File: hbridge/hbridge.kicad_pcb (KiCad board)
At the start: 2 copper layers, 164.5 x 116.5 mm, 8 parts, among them J1 MOSFET1, J2 MOSFET1, J3 MOSFET1, J4 MOSFET1, J5 Driver_in, J6 Driver_in, J7 Driver_in, J8 Driver_in

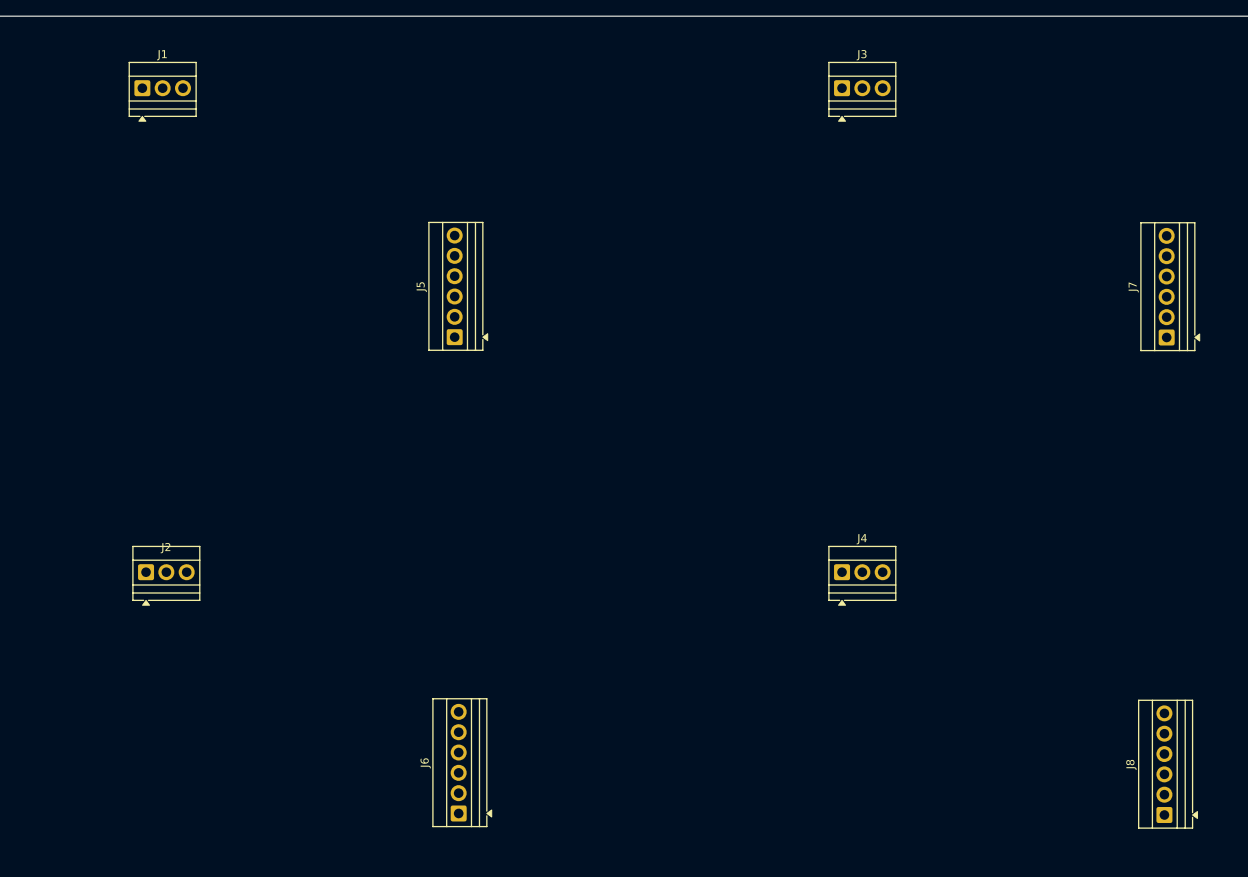
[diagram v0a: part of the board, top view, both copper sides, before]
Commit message: Drivers added to half-bridge.
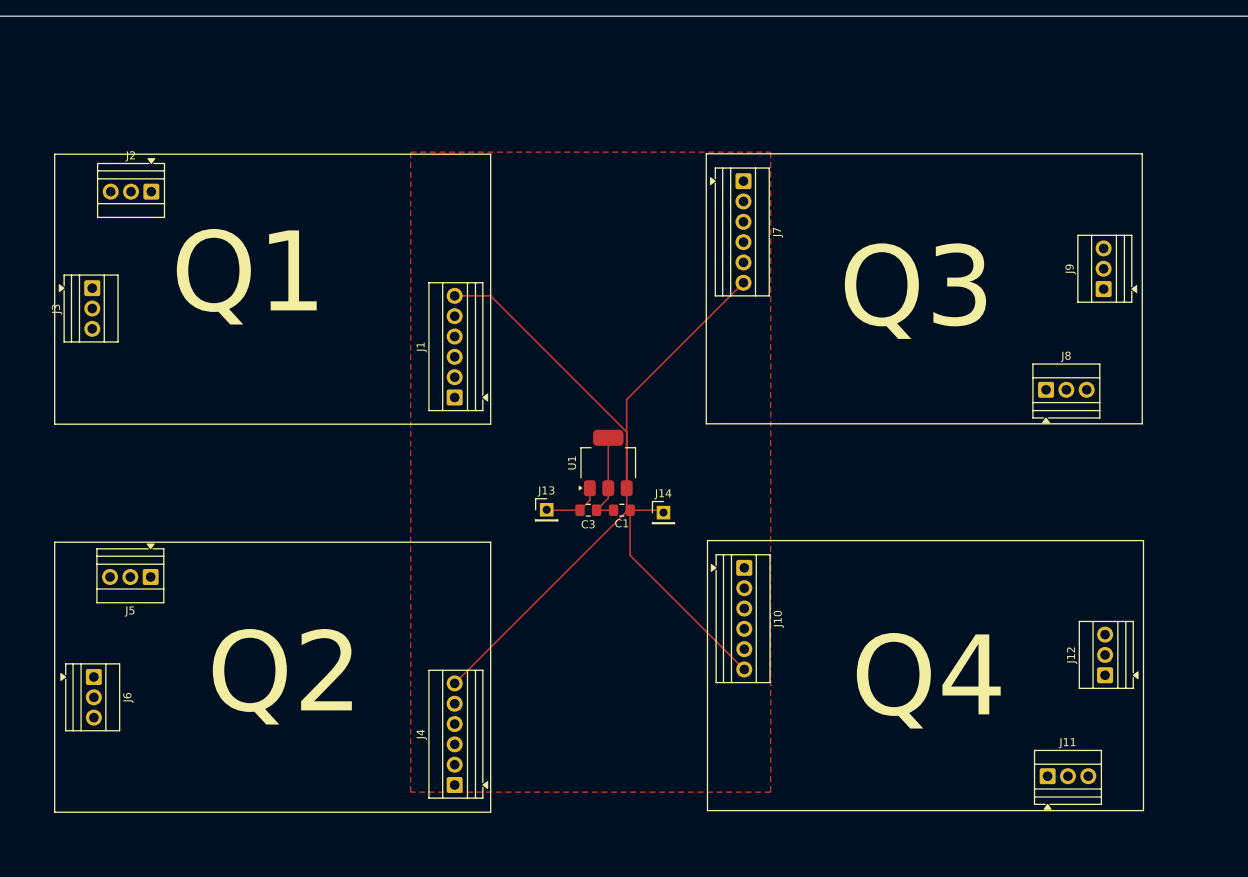
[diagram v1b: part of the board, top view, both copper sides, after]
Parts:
- added C1: C, Capacitor_SMD:C_0805_2012Metric_Pad1.18x1.45mm_HandSolder, F.Cu at (151.4, 84.8)
- added C3: C, Capacitor_SMD:C_0805_2012Metric_Pad1.18x1.45mm_HandSolder, F.Cu at (147.2, 84.8)
- added J10: From_MCU, TerminalBlock:TerminalBlock_Xinya_XY308-2.54-6P_1x06_P2.54mm_Horizontal, F.Cu at (166.7, 92.0)
- added J11: MOSFET_out, TerminalBlock:TerminalBlock_Xinya_XY308-2.54-3P_1x03_P2.54mm_Horizontal, F.Cu at (204.6, 118.0)
- added J12: Conn_01x03, TerminalBlock:TerminalBlock_Xinya_XY308-2.54-3P_1x03_P2.54mm_Horizontal, F.Cu at (211.8, 105.4)
- added J13: Conn_01x01_Socket, Connector_PinHeader_2.54mm:PinHeader_1x01_P2.54mm_Vertical, F.Cu at (142.0, 84.7)
- added J14: Conn_01x01_Socket, Connector_PinHeader_2.54mm:PinHeader_1x01_P2.54mm_Vertical, F.Cu at (156.6, 85.0)
- added J9: Conn_01x03, TerminalBlock:TerminalBlock_Xinya_XY308-2.54-3P_1x03_P2.54mm_Horizontal, F.Cu at (211.6, 57.1)
- added U1: LDO-3.3, Package_TO_SOT_SMD:SOT-223-3_TabPin2, F.Cu at (149.7, 78.8)
- J1, J4: value MOSFET1 -> From_MCU; footprint TerminalBlock:TerminalBlock_Xinya_XY308-2.54-3P_1x03_P2.54mm_Horizontal -> TerminalBlock:TerminalBlock_Xinya_XY308-2.54-6P_1x06_P2.54mm_Horizontal
- J2: value MOSFET1 -> MOSFET_out
- J3: value MOSFET1 -> Conn_01x03
- J5, J8: value Driver_in -> MOSFET_out; footprint TerminalBlock:TerminalBlock_Xinya_XY308-2.54-6P_1x06_P2.54mm_Horizontal -> TerminalBlock:TerminalBlock_Xinya_XY308-2.54-3P_1x03_P2.54mm_Horizontal
- J6: value Driver_in -> Conn_01x03; footprint TerminalBlock:TerminalBlock_Xinya_XY308-2.54-6P_1x06_P2.54mm_Horizontal -> TerminalBlock:TerminalBlock_Xinya_XY308-2.54-3P_1x03_P2.54mm_Horizontal
- J7: value Driver_in -> From_MCU
- moved J3 97.0 mm to (85.2, 57.0), turned to -90 degrees
- moved J7 56.4 mm to (166.6, 43.6), turned to -90 degrees
- moved J4 55.2 mm to (130.5, 119.1), turned to 90 degrees
- moved J8 55.2 mm to (204.4, 69.7), turned to 0 degrees
- moved J1 54.9 mm to (130.5, 70.7), turned to 90 degrees
- moved J6 48.7 mm to (85.4, 105.6), turned to -90 degrees
- moved J5 48.4 mm to (92.5, 93.1), turned to 180 degrees
- moved J2 47.6 mm to (92.6, 44.9), turned to 180 degrees
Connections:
- net Net-(J1-Pin_2) renamed /IN1
- net Net-(J2-Pin_2) renamed /drain1
- net Net-(J4-Pin_2) renamed /IN2
- J1 pad 1: Net-(J1-Pin_1) -> GND_DRV1
- J1 pad 3: Net-(J1-Pin_3) -> /RDY1
- J2 pad 1: Net-(J2-Pin_1) -> /gate1
- J2 pad 3: Net-(J1-Pin_3) -> GND_DRV2
- J3 pad 1: Net-(J3-Pin_1) -> +15_DRV2
- J3 pad 2: Net-(J3-Pin_2) -> GND_DRV2
- J3 pad 3: Net-(J3-Pin_3) -> -15_DRV2
- J4 pad 1: Net-(J4-Pin_1) -> GND_DRV1
- J4 pad 3: Net-(J3-Pin_3) -> /RDY2
- J5 pad 1: unconnected-(J5-Pin_1-Pad1) -> /gate2
- J5 pad 2: Net-(J1-Pin_1) -> /drain2
- J5 pad 3: unconnected-(J5-Pin_3-Pad3) -> GND_DRV2
- J6 pad 1: unconnected-(J6-Pin_1-Pad1) -> +15_DRV2
- J6 pad 2: Net-(J2-Pin_1) -> GND_DRV2
- J6 pad 3: unconnected-(J6-Pin_3-Pad3) -> -15_DRV2
- J7 pad 1: unconnected-(J7-Pin_1-Pad1) -> GND_DRV1
- J7 pad 2: Net-(J3-Pin_1) -> /IN3
- J7 pad 3: unconnected-(J7-Pin_3-Pad3) -> /RDY3
- J7 pad 4: unconnected-(J7-Pin_4-Pad4) -> /FLT3
- J7 pad 5: unconnected-(J7-Pin_5-Pad5) -> /EN3
- J7 pad 6: unconnected-(J7-Pin_6-Pad6) -> +3V3_DRV1
- J8 pad 1: unconnected-(J8-Pin_1-Pad1) -> /gate3
- J8 pad 2: Net-(J4-Pin_1) -> /drain3
- J8 pad 3: unconnected-(J8-Pin_3-Pad3) -> GND_DRV2
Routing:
- net +3V3_DRV1: track 0.00 -> 131.2 mm
- net GND_DRV1: track 0.00 -> 11.8 mm
- net Net-(J13-Pin_1): track 0.00 -> 7.45 mm
- added copper zone on F.Cu, net GND_DRV1
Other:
- board text added: "Q1"
- board text added: "Q2"
- board text added: "Q3"
- board text added: "Q4"

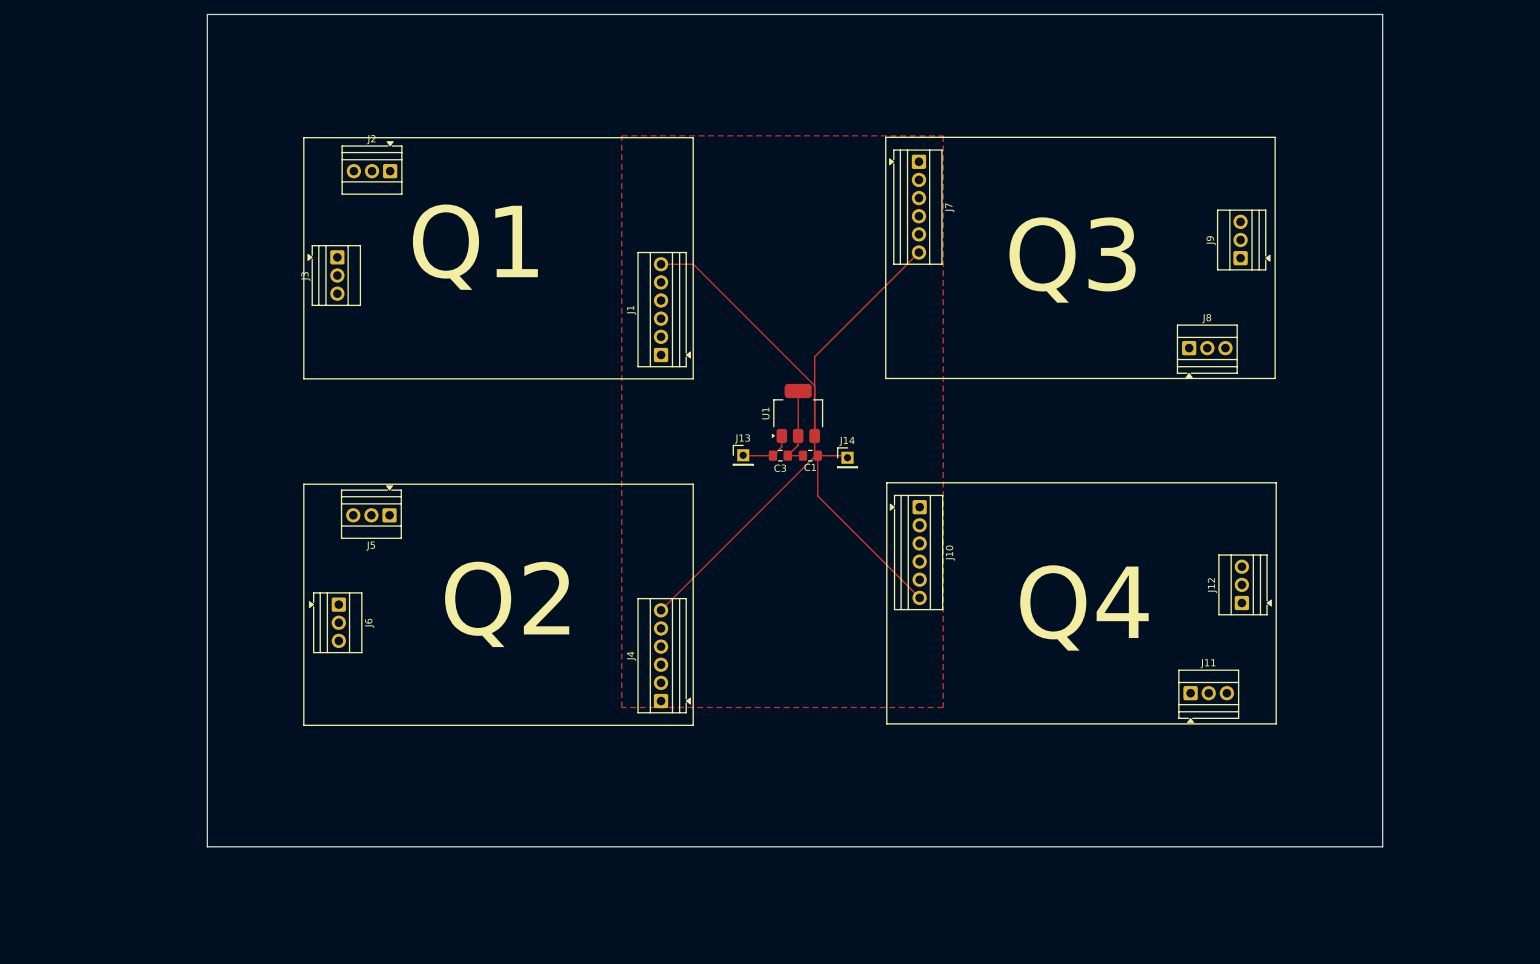
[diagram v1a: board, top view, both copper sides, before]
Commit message: Half bridge power to PCB added.
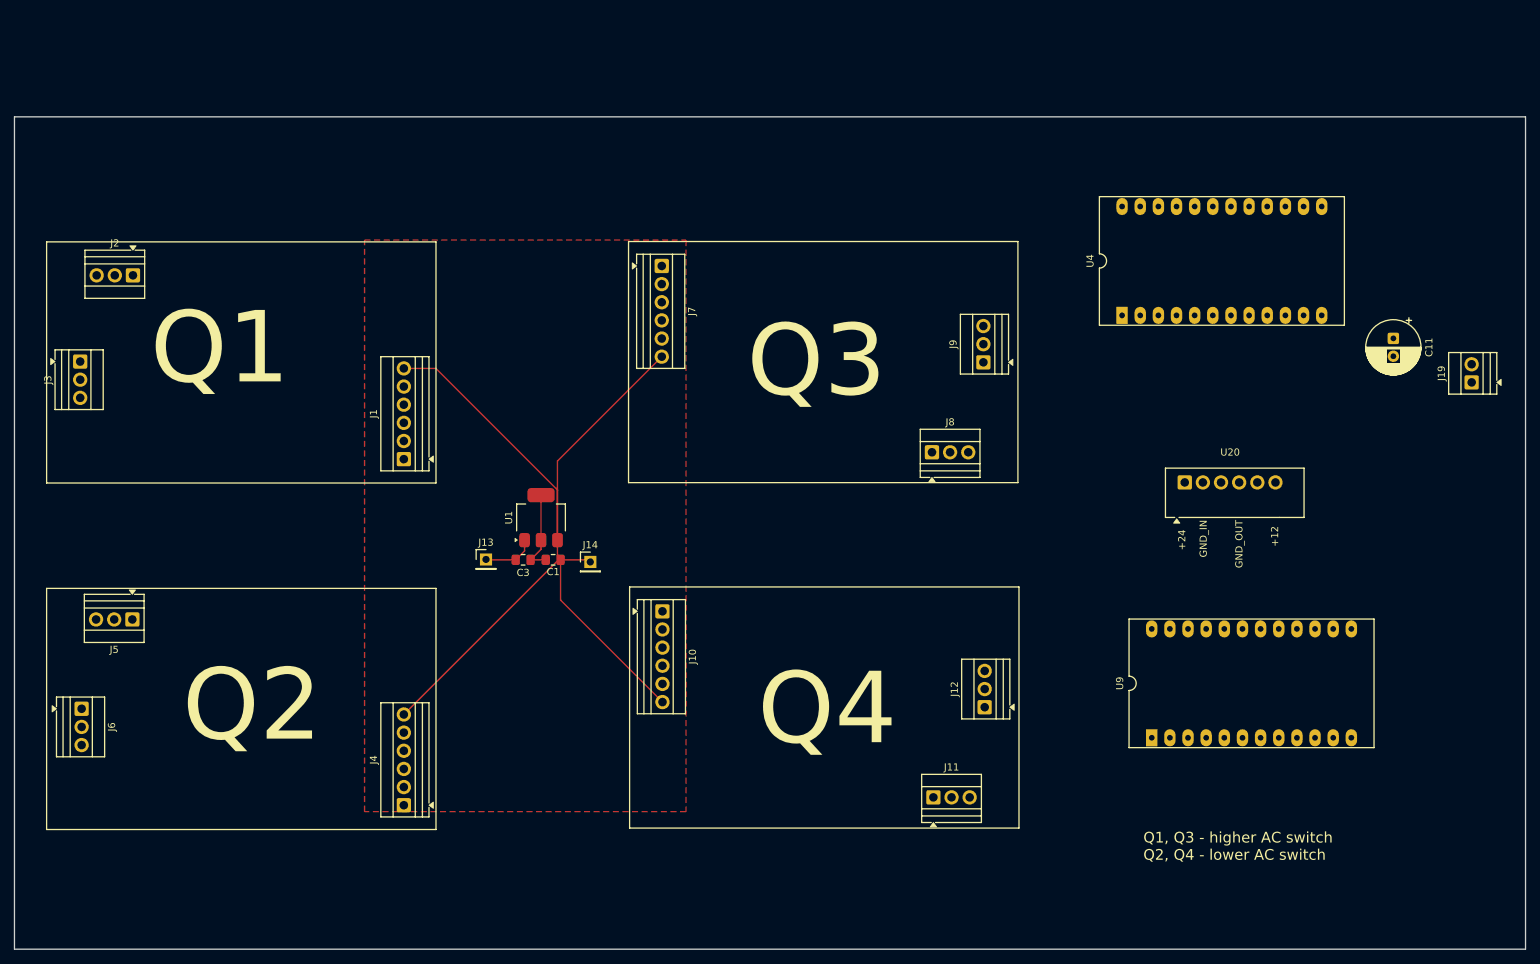
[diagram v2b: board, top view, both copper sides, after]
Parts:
- added C11: 100-220uF/50V, Capacitor_THT:CP_Radial_D7.5mm_P2.50mm, F.Cu at (233.0, 68.3)
- added J19: 24V, TerminalBlock:TerminalBlock_Xinya_XY308-2.54-2P_1x02_P2.54mm_Horizontal, F.Cu at (244.0, 74.5)
- added U20: B2412S-2WR3, TerminalBlock:TerminalBlock_Xinya_XY308-2.54-6P_1x06_P2.54mm_Horizontal, F.Cu at (203.8, 88.5)
- added U4: AM6TW-2415DZ, Package_DIP:DIP-24_18.0mmx34.29mm_W15.24mm_LongPads, F.Cu at (195.0, 65.1)
- added U9: AM6TW-2415DZ, Package_DIP:DIP-24_18.0mmx34.29mm_W15.24mm_LongPads, F.Cu at (199.2, 124.2)
- moved J6 38.8 mm to (49.4, 120.2)
- moved C1 38.8 mm to (115.4, 99.3)
- moved J1 38.8 mm to (94.5, 85.2)
- moved J10 38.8 mm to (130.7, 106.5)
- moved J11 38.8 mm to (168.6, 132.6)
- moved J12 38.8 mm to (175.8, 120.0)
- moved J13 38.8 mm to (106.0, 99.3)
- moved J14 38.8 mm to (120.6, 99.6)
- moved J3 38.8 mm to (49.2, 71.6)
- moved J4 38.8 mm to (94.5, 133.7)
- moved J5 38.8 mm to (56.5, 107.7)
- moved J7 38.8 mm to (130.6, 58.2)
- moved J8 38.8 mm to (168.4, 84.3)
- moved J9 38.8 mm to (175.6, 71.7)
- moved J2 38.8 mm to (56.6, 59.5)
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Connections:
- net /EN1 renamed /драйверы/EN1
- net /EN2 renamed /драйверы/EN2
- net /EN3 renamed /драйверы/EN3
- net /EN4 renamed /драйверы/EN4
- net /FLT1 renamed /драйверы/FLT1
- net /FLT2 renamed /драйверы/FLT2
- net /FLT3 renamed /драйверы/FLT3
- net /FLT4 renamed /драйверы/FLT4
- net /IN1 renamed /драйверы/IN1
- net /IN2 renamed /драйверы/IN2
- net /IN3 renamed /драйверы/IN3
- net /IN4 renamed /драйверы/IN4
- net /RDY1 renamed /драйверы/RDY1
- net /RDY2 renamed /драйверы/RDY2
- net /RDY3 renamed /драйверы/RDY3
- net /RDY4 renamed /драйверы/RDY4
- net /drain1 renamed /драйверы/drain1
- net /drain2 renamed /драйверы/drain2
- net /drain3 renamed /драйверы/drain3
- net /drain4 renamed /драйверы/drain4
- net /gate1 renamed /драйверы/gate1
- net /gate2 renamed /драйверы/gate2
- net /gate3 renamed /драйверы/gate3
- net /gate4 renamed /драйверы/gate4
- net Net-(J13-Pin_1) renamed +12V
- J12 pad 1: +15_DRV2 -> +15_DRV2_L
- J12 pad 2: GND_DRV2 -> GND_DRV2_L
- J12 pad 3: -15_DRV2 -> -15_DRV2_L
- J3 pad 1: +15_DRV2 -> +15_DRV2_H
- J3 pad 2: GND_DRV2 -> GND_DRV2_H
- J3 pad 3: -15_DRV2 -> -15_DRV2_H
- J6 pad 1: +15_DRV2 -> +15_DRV2_L
- J6 pad 2: GND_DRV2 -> GND_DRV2_L
- J6 pad 3: -15_DRV2 -> -15_DRV2_L
- J9 pad 1: +15_DRV2 -> +15_DRV2_H
- J9 pad 2: GND_DRV2 -> GND_DRV2_H
- J9 pad 3: -15_DRV2 -> -15_DRV2_H
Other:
- board size 164.5 x 116.5 mm -> 211.5 x 116.5 mm
- board text added: "+12"
- board text added: "+24"
- board text added: "GND_IN"
- board text added: "GND_OUT"
- board text added: "Q1, Q3 - higher AC switch Q2, Q4 - lower AC switch"

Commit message: PCB minor changes.
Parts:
- moved C11 20.2 mm to (226.0, 87.2)
- moved J19 15.3 mm to (243.2, 89.8)
- moved U20 13.5 mm to (191.6, 94.2)
- moved U9 7.70 mm to (191.5, 125.1)
- moved U4 3.54 mm to (191.5, 65.6)
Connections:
- J11 pad 3: GND_DRV2 -> GND_DRV2_L
- J2 pad 3: GND_DRV2 -> GND_DRV2_H
- J5 pad 3: GND_DRV2 -> GND_DRV2_L
- J8 pad 3: GND_DRV2 -> GND_DRV2_H
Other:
- board size 211.5 x 116.5 mm -> 211.5 x 106.7 mm
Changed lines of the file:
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@@
 			(layers "*.Cu" "*.Mask")
 			(remove_unused_layers no)
-			(net "GND_DRV2")
+			(net "GND_DRV2_H")
 			(pinfunction "Pin_3_3")
 			(pintype "passive")
@@
 	(footprint "TerminalBlock:TerminalBlock_Xinya_XY308-2.54-2P_1x02_P2.54mm_Horizontal"
 		(layer "F.Cu")
-		(at 243.96 74.5 90)
+		(at 243.2175 89.775 90)
 		(descr "Terminal Block Xinya XY308-2.54-2P, 2 pins, pitch 2.54mm, size 5.58x6.5mm, drill diameter 1.2mm, pad diameter 2mm, http://www.xinyaelectronic.com/product/xy308-254")
 		(tags "THT Terminal Block Xinya XY308-2.54-2P pitch 2.54mm size 5.58x6.5mm drill 1.2mm pad 2mm")
@@
 			(layers "*.Cu" "*.Mask")
 			(remove_unused_layers no)
-			(net "GND_DRV2")
+			(net "GND_DRV2_L")
 			(pinfunction "Pin_3_3")
 			(pintype "passive")
@@
 	(footprint "Package_DIP:DIP-24_18.0mmx34.29mm_W15.24mm_LongPads"
 		(layer "F.Cu")
-		(at 199.18 124.24 90)
+		(at 191.53 125.12 90)
 		(descr "24-lead though-hole mounted DIP package, row spacing 15.24 mm (600 mils) https://www.mouser.at/datasheet/2/389/m48t02-1849963.pdf")
 		(tags "THT DIP DIL PDIP 2.54mm 15.24mm 600mil PCDIP24 CAPHAT M48T02 M48T12 M48Z02 M48Z12")
@@
 	(footprint "Capacitor_THT:CP_Radial_D7.5mm_P2.50mm"
 		(layer "F.Cu")
-		(at 233 68.338606 -90)
+		(at 226 87.25 -90)
 		(descr "CP, Radial series, Radial, pin pitch=2.50mm, diameter=7.5mm, height=8mm, Electrolytic Capacitor")
 		(tags "CP Radial series Radial pin pitch 2.50mm diameter 7.5mm height 8mm Electrolytic Capacitor")
@@
 	(footprint "TerminalBlock:TerminalBlock_Xinya_XY308-2.54-6P_1x06_P2.54mm_Horizontal"
 		(layer "F.Cu")
-		(at 203.8 88.5)
+		(at 191.55 94.25)
 		(descr "Terminal Block Xinya XY308-2.54-6P, 6 pins, pitch 2.54mm, size 15.7x6.5mm, drill diameter 1.2mm, pad diameter 2mm, http://www.xinyaelectronic.com/product/xy308-254")
 		(tags "THT Terminal Block Xinya XY308-2.54-6P pitch 2.54mm size 15.7x6.5mm drill 1.2mm pad 2mm")
@@
 			(layers "*.Cu" "*.Mask")
 			(remove_unused_layers no)
-			(net "GND_DRV2")
+			(net "GND_DRV2_H")
 			(pinfunction "Pin_3_3")
 			(pintype "passive")
@@
 	(footprint "Package_DIP:DIP-24_18.0mmx34.29mm_W15.24mm_LongPads"
 		(layer "F.Cu")
-		(at 195.03 65.12 90)
+		(at 191.53 65.62 90)
 		(descr "24-lead though-hole mounted DIP package, row spacing 15.24 mm (600 mils) https://www.mouser.at/datasheet/2/389/m48t02-1849963.pdf")
 		(tags "THT DIP DIL PDIP 2.54mm 15.24mm 600mil PCDIP24 CAPHAT M48T02 M48T12 M48Z02 M48Z12")
@@
 			(layers "*.Cu" "*.Mask")
 			(remove_unused_layers no)
-			(net "GND_DRV2")
+			(net "GND_DRV2_L")
 			(pinfunction "Pin_3_3")
 			(pintype "passive")
@@
 	(gr_rect
 		(start 40 37.33)
-		(end 251.5 153.83)
+		(end 251.5 144)
 		(stroke
 			(width 0.05)
@@
 		(layer "Edge.Cuts")
 	)
+	(gr_line
+		(start 24.75 95.75)
+		(end 180.25 95.75)
+		(stroke
+			(width 0.1)
+			(type default)
+		)
+		(layer "F.Fab")
+	)
 	(gr_rect
 		(start 45.8 69.98)
@@
 	)
 	(gr_text "+24"
-		(at 204 98 90)
+		(at 191.75 103.75 90)
 		(layer "F.SilkS")
 		(effects
@@
 	)
 	(gr_text "GND_IN"
-		(at 207 99 90)
+		(at 194.75 104.75 90)
 		(layer "F.SilkS")
 		(effects
@@
 	)
 	(gr_text "GND_OUT"
-		(at 212 100.5 90)
+		(at 199.75 106.25 90)
 		(layer "F.SilkS")
 		(effects
@@
 	)
 	(gr_text "+12"
-		(at 217 97.5 90)
+		(at 204.75 103.25 90)
 		(layer "F.SilkS")
 		(effects
@@
 	)
 	(gr_text "Q1, Q3 - higher AC switch\nQ2, Q4 - lower AC switch"
-		(at 198 141.5 0)
+		(at 197 138.5 0)
 		(layer "F.SilkS")
 		(effects
@@
 	)
 	(segment
-		(start 113.7 97.8675)
-		(end 112.2375 99.33)
+		(start 111.4 98.0925)
+		(end 110.1625 99.33)
 		(width 0.2)
 		(layer "F.Cu")
-		(net "GND_DRV1")
+		(net "+12V")
 	)
 	(segment
-		(start 112.2375 99.33)
-		(end 114.3625 99.33)
+		(start 106.05 99.33)
+		(end 106 99.28)
 		(width 0.2)
 		(layer "F.Cu")
-		(net "GND_DRV1")
+		(net "+12V")
 	)
 	(segment
-		(start 113.7 96.58)
-		(end 113.7 90.28)
+		(start 111.4 96.58)
+		(end 111.4 98.0925)
 		(width 0.2)
 		(layer "F.Cu")
-		(net "GND_DRV1")
+		(net "+12V")
 	)
 	(segment
-		(start 113.7 96.58)
-		(end 113.7 97.8675)
+		(start 110.1625 99.33)
+		(end 106.05 99.33)
 		(width 0.2)
 		(layer "F.Cu")
-		(net "GND_DRV1")
+		(net "+12V")
 	)
 	(segment
-		(start 111.4 98.0925)
-		(end 110.1625 99.33)
+		(start 113.7 97.8675)
+		(end 112.2375 99.33)
 		(width 0.2)
 		(layer "F.Cu")
-		(net "+12V")
+		(net "GND_DRV1")
 	)
 	(segment
-		(start 106.05 99.33)
-		(end 106 99.28)
+		(start 112.2375 99.33)
+		(end 114.3625 99.33)
 		(width 0.2)
 		(layer "F.Cu")
-		(net "+12V")
+		(net "GND_DRV1")
 	)
 	(segment
-		(start 111.4 96.58)
-		(end 111.4 98.0925)
+		(start 113.7 96.58)
+		(end 113.7 90.28)
 		(width 0.2)
 		(layer "F.Cu")
-		(net "+12V")
+		(net "GND_DRV1")
 	)
 	(segment
-		(start 110.1625 99.33)
-		(end 106.05 99.33)
+		(start 113.7 96.58)
+		(end 113.7 97.8675)
 		(width 0.2)
 		(layer "F.Cu")
-		(net "+12V")
+		(net "GND_DRV1")
 	)
 	(zone
